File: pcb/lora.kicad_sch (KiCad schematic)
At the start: 24 parts, among them U5 SX1262IMLTRT, U6 BGS12WN6E6327, Y3 KT2520K-T

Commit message: buck converter and updates
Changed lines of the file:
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@@
+		)
+	)
+	(label "VBAT_DEC"
+		(at 109.22 71.12 0)
+		(effects
+			(font
+				(size 1.27 1.27)
+			)
+			(justify left bottom)
+		)
+	)
+	(label "VBAT_DEC"
+		(at 102.87 45.72 0)
+		(effects
+			(font
+				(size 1.27 1.27)
+			)
+			(justify left bottom)
 		)
 	)

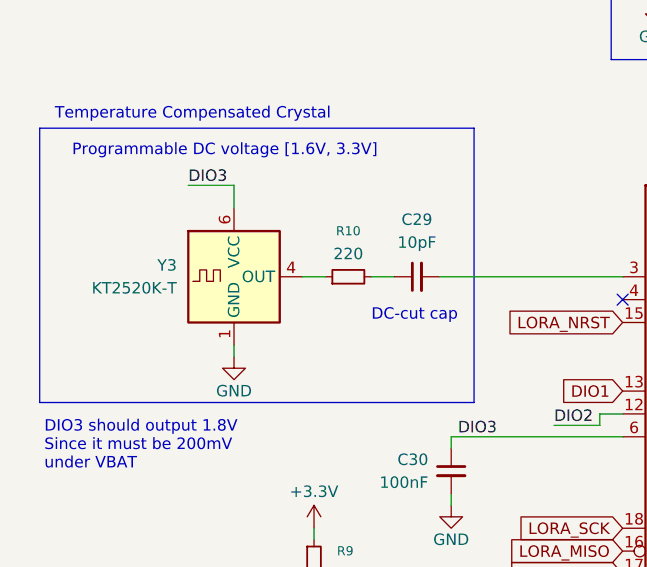
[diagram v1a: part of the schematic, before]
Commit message: switch TCXO, laid out from ref design from nordic
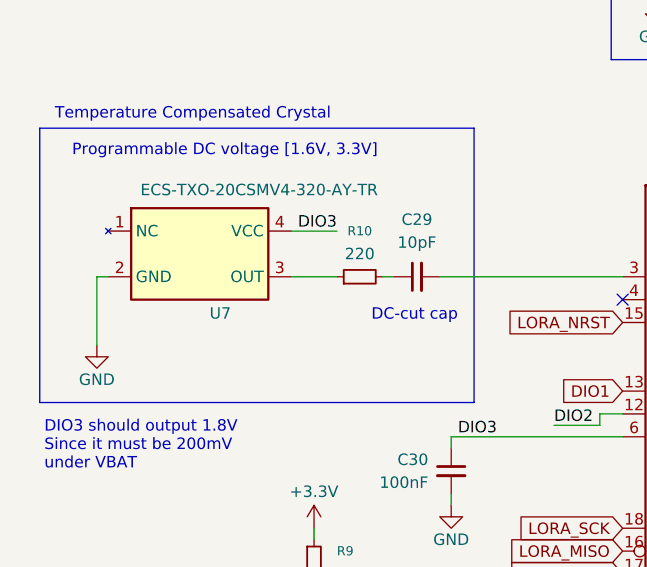
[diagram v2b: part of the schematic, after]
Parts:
- removed Y3: KT2520K-T, Oscillator:Oscillator_SMD_Kyocera_2520-6Pin_2.5x2.0mm, symbol Oscillator:KT2520K-T
- added U7: ECS-TXO-20CSMV4-320-AY-TR, footprints:Oscillator_SMD_ECS_2016, symbol ECS-TXO-20CSMV4:ECS-TXO-20CSMV4-320-AY-TR
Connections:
- net DIO3: now also U7.4 (VCC)
- net GND: now also U7.2 (GND)
- net at R10.1: now also U7.3 (OUT)
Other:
- moved on the sheet: R10
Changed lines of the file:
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@@
 	(wire
 		(pts
+			(xy 38.1 85.09) (xy 39.37 85.09)
+		)
+		(stroke
+			(width 0)
+			(type default)
+		)
+	)
+	(wire
+		(pts
 			(xy 252.73 106.68) (xy 260.35 106.68)
 		)
@@
 	(wire
 		(pts
-			(xy 68.58 85.09) (xy 71.12 85.09)
+			(xy 69.85 85.09) (xy 71.12 85.09)
 		)
 		(stroke
@@
 	(wire
 		(pts
+			(xy 59.69 85.09) (xy 64.77 85.09)
+		)
+		(stroke
+			(width 0)
+			(type default)
+		)
+	)
+	(wire
+		(pts
 			(xy 109.22 71.12) (xy 116.84 71.12)
 		)
@@
 	(wire
 		(pts
-			(xy 53.34 93.98) (xy 53.34 92.71)
-		)
-		(stroke
-			(width 0)
-			(type default)
-		)
-	)
-	(wire
-		(pts
 			(xy 106.68 69.85) (xy 106.68 71.12)
 		)
@@
 	(wire
 		(pts
-			(xy 53.34 74.93) (xy 53.34 77.47)
-		)
-		(stroke
-			(width 0)
-			(type default)
-		)
-	)
-	(wire
-		(pts
 			(xy 240.03 106.68) (xy 243.84 106.68)
 		)
@@
 	(wire
 		(pts
-			(xy 48.26 74.93) (xy 53.34 74.93)
+			(xy 64.77 80.01) (xy 59.69 80.01)
 		)
 		(stroke
@@
 	(wire
 		(pts
-			(xy 60.96 85.09) (xy 63.5 85.09)
+			(xy 109.22 71.12) (xy 109.22 72.39)
 		)
 		(stroke
@@
 	(wire
 		(pts
-			(xy 109.22 71.12) (xy 109.22 72.39)
+			(xy 38.1 85.09) (xy 38.1 92.71)
 		)
 		(stroke
@@
 	)
 	(label "DIO3"
-		(at 48.26 74.93 0)
+		(at 64.77 80.01 180)
 		(effects
 			(font
 				(size 1.27 1.27)
 			)
-			(justify left bottom)
+			(justify right bottom)
 		)
 	)
@@
 	(symbol
 		(lib_id "power:GND")
-		(at 53.34 93.98 0)
+		(at 38.1 92.71 0)
 		(unit 1)
 		(body_style 1)
@@
 		(dnp no)
 		(property "Reference" "#PWR040"
-			(at 53.34 100.33 0)
+			(at 38.1 99.06 0)
 			(hide yes)
 			(show_name no)
@@
 		)
 		(property "Value" "GND"
-			(at 53.34 97.79 0)
+			(at 38.1 96.52 0)
 			(show_name no)
 			(do_not_autoplace no)
@@
 		)
 		(property "Footprint" ""
-			(at 53.34 93.98 0)
+			(at 38.1 92.71 0)
 			(hide yes)
 			(show_name no)
@@
 		)
 		(property "Datasheet" ""
-			(at 53.34 93.98 0)
+			(at 38.1 92.71 0)
 			(hide yes)
 			(show_name no)
@@
 		)
 		(property "Description" "Power symbol creates a global label with name \"GND\" , ground"
-			(at 53.34 93.98 0)
+			(at 38.1 92.71 0)
 			(hide yes)
 			(show_name no)
@@
 	(symbol
 		(lib_id "Device:R_Small")
-		(at 66.04 85.09 90)
+		(at 67.31 85.09 90)
 		(unit 1)
 		(body_style 1)
@@
 		(fields_autoplaced yes)
 		(property "Reference" "R10"
-			(at 66.04 80.01 90)
+			(at 67.31 80.01 90)
 			(show_name no)
 			(do_not_autoplace no)
@@
 		)
 		(property "Value" "220"
-			(at 66.04 82.55 90)
+			(at 67.31 82.55 90)
 			(show_name no)
 			(do_not_autoplace no)
@@
 		)
 		(property "Footprint" "Resistor_SMD:R_0603_1608Metric"
-			(at 66.04 85.09 0)
+			(at 67.31 85.09 0)
 			(hide yes)
 			(show_name no)
@@
 		)
 		(property "Datasheet" ""
-			(at 66.04 85.09 0)
+			(at 67.31 85.09 0)
 			(hide yes)
 			(show_name no)
@@
 		)
 		(property "Description" "Resistor, small symbol"
-			(at 66.04 85.09 0)
+			(at 67.31 85.09 0)
 			(hide yes)
 			(show_name no)
@@
 	)
 	(symbol
-		(lib_id "Oscillator:KT2520K-T")
-		(at 53.34 85.09 0)
-		(unit 1)
-		(body_style 1)
-		(exclude_from_sim no)
-		(in_bom yes)
-		(on_board yes)
-		(in_pos_files yes)
-		(dnp no)
-		(fields_autoplaced yes)
-		(property "Reference" "Y3"
-			(at 46.99 83.8199 0)
-			(show_name no)
-			(do_not_autoplace no)
-			(effects
-				(font
-					(size 1.27 1.27)
-				)
-				(justify right)
-			)
-		)
-		(property "Value" "KT2520K-T"
-			(at 46.99 86.3599 0)
-			(show_name no)
-			(do_not_autoplace no)
-			(effects
-				(font
-					(size 1.27 1.27)
-				)
-				(justify right)
-			)
-		)
-		(property "Footprint" "Oscillator:Oscillator_SMD_Kyocera_2520-6Pin_2.5x2.0mm"
-			(at 50.8 87.63 0)
-			(hide yes)
-			(show_name no)
-			(do_not_autoplace no)
-			(effects
-				(font
-					(size 1.27 1.27)
-				)
-			)
-		)
-		(property "Datasheet" "https://global.kyocera.com/prdct/electro/product/pdf/kt2520_e.pdf"
-			(at 53.34 85.09 0)
-			(hide yes)
-			(show_name no)
-			(do_not_autoplace no)
-			(effects
-				(font
-					(size 1.27 1.27)
-				)
-			)
-		)
-		(property "Description" "10-60MHz Temperature Compensated Crystal Oscillator, Kyocera 2520"
-			(at 53.34 85.09 0)
-			(hide yes)
-			(show_name no)
-			(do_not_autoplace no)
-			(effects
-				(font
-					(size 1.27 1.27)
-				)
-			)
-		)
-		(pin "1"
-		)
-		(pin "6"
-		)
-		(pin "2"
-		)
-		(pin "5"
-		)
-		(pin "3"
-		)
-		(pin "4"
-		)
-		(instances
-			(project "pcb"
-				(path "/52b1b5de-c493-4cfe-b90b-d072cb2fb98d/a63ec2f7-32f8-4190-b7fd-dd0d9e74a442"
-					(reference "Y3")
-					(unit 1)
-				)
-			)
-		)
-	)
-	(symbol
 		(lib_id "Device:R_Small")
 		(at 222.25 138.43 90)
@@
 					(unit 1)
 				)
+			)
+		)
+	)
+	(symbol
+		(lib_id "ECS-TXO-20CSMV4:ECS-TXO-20CSMV4-320-AY-TR")
+		(at 49.53 82.55 0)
+		(unit 1)
+		(body_style 1)
+		(exclude_from_sim no)
+		(in_bom yes)
+		(on_board yes)
+		(in_pos_files yes)
+		(dnp no)
+		(property "Reference" "U7"
+			(at 51.816 89.154 0)
+			(show_name no)
+			(do_not_autoplace no)
+			(effects
+				(font
+					(size 1.27 1.27)
+				)
+			)
+		)
+		(property "Value" "ECS-TXO-20CSMV4-320-AY-TR"
+			(at 56.134 75.438 0)
+			(show_name no)
+			(do_not_autoplace no)
+			(effects
+				(font
+					(size 1.27 1.27)
+				)
+			)
+		)
+		(property "Footprint" "footprints:Oscillator_SMD_ECS_2016"
+			(at 49.53 92.71 0)
+			(hide yes)
+			(show_name no)
+			(do_not_autoplace no)
+			(effects
+				(font
+					(size 1.27 1.27)
+				)
+			)
+		)
+		(property "Datasheet" "https://ecsxtal.com/store/pdf/ECS-TXO-20CSMV4.pdf"
+			(at 49.53 95.25 0)
+			(hide yes)
+			(show_name no)
+			(do_not_autoplace no)
+			(effects
+				(font
+					(size 1.27 1.27)
+				)
+			)
+		)
+		(property "Description" ""
+			(at 49.53 82.55 0)
+			(hide yes)
+			(show_name no)
+			(do_not_autoplace no)
+			(effects
+				(font
+					(size 1.27 1.27)
+				)
+			)
+		)
+		(pin "3"
+		)
+		(pin "1"
+		)
+		(pin "2"
+		)
+		(pin "4"
+		)
+		(instances
+			(project "pcb"
+				(path "/52b1b5de-c493-4cfe-b90b-d072cb2fb98d/a63ec2f7-32f8-4190-b7fd-dd0d9e74a442"
+					(reference "U7")
+					(unit 1)
+				)

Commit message: V2
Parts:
- C40: renamed from C31; footprint Capacitor_SMD:C_0805_2012Metric -> Capacitor_SMD:C_0603_1608Metric
- C45: renamed from C33; footprint Capacitor_SMD:C_0805_2012Metric -> Capacitor_SMD:C_0603_1608Metric
- renumbered C32 to C41, C34 to C42, C36 to C43, C29 to C44, C35 to C46, C30 to C47, C38 to C48, C39 to C49, C40 to C50, C37 to C51, L9 to L10, L7 to L8, L8 to L9, R11 to R14, R10 to R15, R9 to R16, R12 to R17, U7 to U6, U5 to U7, U6 to U8
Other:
- note added: "Stitching Via Distance L=wavelength/20 for 915MHz on an outer layer: L = 9mm Resonant Frequencies at 1.38GHz and 2.74GHz L = 2.5mm works best to suppress resonant frequencies, which would pass through a 9mm stitching distance"
- note removed: "Stitching Via Distance L=wavelength/20 for 915MHz on an outer layer: L = 9mm"

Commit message: V2 fixup
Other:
- note added: "CPWG: 0.37mm Trace Width 0.22mm Gap ~49.9 ohm (D_{K} = 4.2 with 7628 prepreg) 7628 prepreg thickness is 0.2104mm according to JLCPCB Opening soldermask above the CPWG increases performance but can lead to oxidation of the copper. The difference in manufacturing loss tolerance is usually +-2 ohms. Oxidation can corrode the trace and lead to way worse impedance control over time, so I'm chosing to 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"
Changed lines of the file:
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@@
 		(title "915MHz LoRa Modem")
 		(date "2026-10-09")
-		(rev "1")
+		(rev "2")
 		(company "Dylan DiBeneditto")
 	)
@@
 		)
 	)
+	(text "CPWG:\n0.37mm Trace Width\n0.22mm Gap\n~49.9 ohm\n(D_{K} = 4.2 with 7628 prepreg)\n7628 prepreg thickness is 0.2104mm according to JLCPCB\n\nOpening soldermask above the CPWG increases performance\nbut can lead to oxidation of the copper. The difference \nin manufacturing loss tolerance is usually +-2 ohms.\n\nOxidation can corrode the trace and lead to way worse impedance\ncontrol over time, so I'm chosing to go without it."
+		(exclude_from_sim no)
+		(at 92.456 180.848 0)
+		(effects
+			(font
+				(size 1.27 1.27)
+			)
+			(justify left)
+		)
+	)

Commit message: revision 3
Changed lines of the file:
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@@
 		(title "915MHz LoRa Modem")
 		(date "2026-10-09")
-		(rev "2")
+		(rev "3")
 		(company "Dylan DiBeneditto")
 	)
@@
 	(global_label "DIO1"
 		(shape input)
-		(at 199.39 35.56 180)
+		(at 228.6 27.94 180)
 		(fields_autoplaced yes)
 		(effects
@@
 		)
 		(property "Intersheetrefs" "${INTERSHEET_REFS}"
-			(at 191.99 35.56 0)
+			(at 221.2 27.94 0)
 			(hide yes)
 			(show_name no)
@@
 	(hierarchical_label "DIO1"
 		(shape bidirectional)
-		(at 199.39 35.56 0)
-		(effects
-			(font
+		(at 228.6 27.94 0)
+		(effects
+			(font
